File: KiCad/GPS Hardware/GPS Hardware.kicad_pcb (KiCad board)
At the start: 4 copper layers, 50 x 50 mm, 74 parts, among them J1 USB_C_Receptacle_USB2.0, J2 Conn_01x06_Male, J3 Conn_Coaxial, J4 SIM8051-6-0-14-01-X-REVD, J5 B2B-XH-A(LF)(SN), Q1 BC847, Q2 BC847, Q3 BSS84, U1 ESD122DMX, U10 ublox_SAM-M8Q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

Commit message: Update to PC
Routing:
- net VCC_GPS: track 29.3 -> 33.1 mm

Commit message: Update to laptop
You need to finish gnd via placement
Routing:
- net Net-(J1-PadB5): track 0.00 -> 2.69 mm
- net GND: vias 22 -> 23
- net D-: vias 0 -> 1

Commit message: Update to PC Remember to double-check pads
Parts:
- moved C31 0.76 mm to (118.7, 64.3)
- moved D6 0.55 mm to (119.9, 64.2)
- moved C30 0.52 mm to (120.8, 64.2)
- moved TH1 0.32 mm to (103.5, 71.9)
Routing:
- net GND: track 13.0 -> 21.9 mm, vias 23 -> 111
- net D+: track 4.98 -> 10.2 mm
- net D-: track 5.93 -> 8.94 mm, vias 1 -> 2
- net Net-(C10-Pad1): track 0.00 -> 2.09 mm
- net VSIM: track 26.9 -> 25.3 mm
- net SCL_Power: track 84.0 -> 85.1 mm
- net SDA_Power: track 81.5 -> 82.5 mm
- net INT_Power: track 62.3 -> 63.1 mm
- net +3V3: vias 8 -> 10

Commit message: Update from laptop
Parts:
- moved C28 0.51 mm to (134.6, 62.9)
- moved D4 0.51 mm to (135.6, 62.9)
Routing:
- net +3V3: track 10.3 -> 13.8 mm, vias 10 -> 14
- net VCC_GPS: track 33.1 -> 36.4 mm
- net GND: track 21.9 -> 23.9 mm, vias 111 -> 114

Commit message: Update from university
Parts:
- moved TH1 0.22 mm to (103.3, 71.9)
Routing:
- net Net-(J3-Pad1): track 0.00 -> 3.82 mm
- net GND: track 23.9 -> 22.6 mm, vias 114 -> 177
- net CLK: track 41.6 -> 40.5 mm
- net RESET_Cellular: vias 2 -> 3

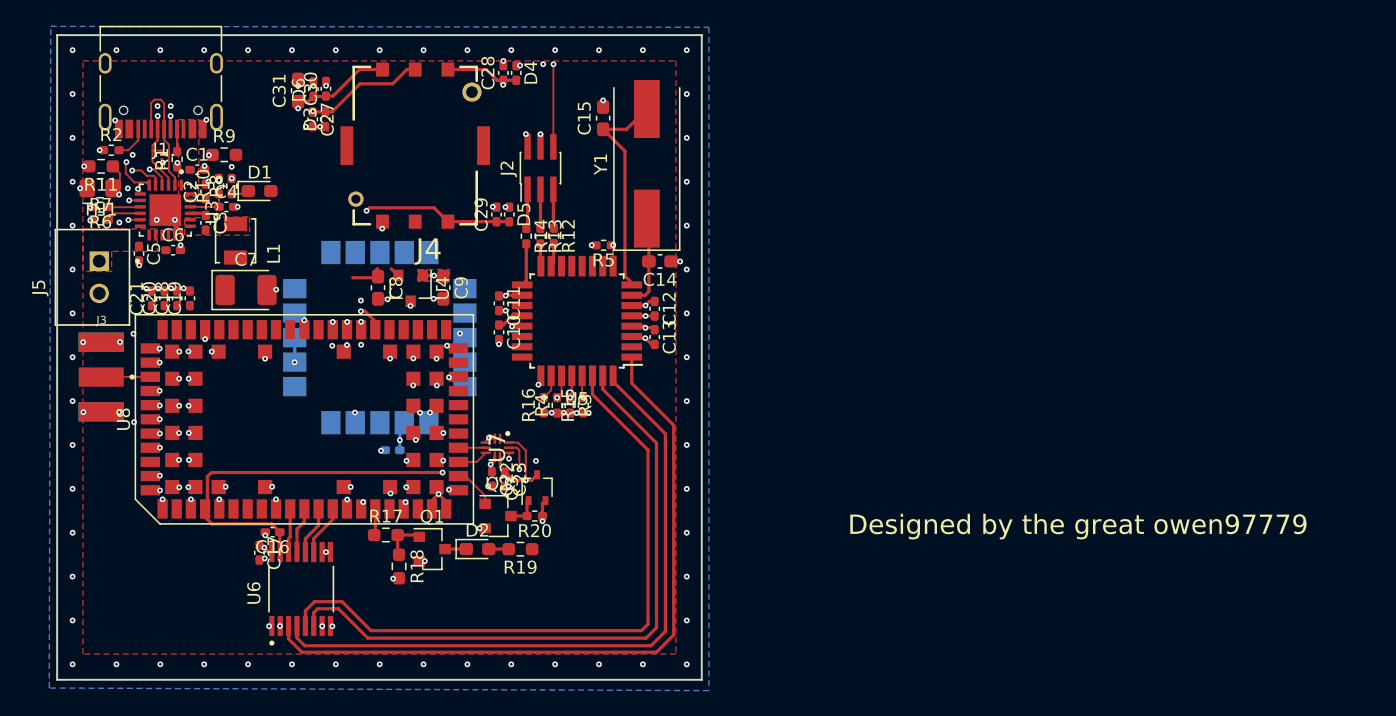
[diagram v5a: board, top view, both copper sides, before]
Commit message: Updated silkscreen
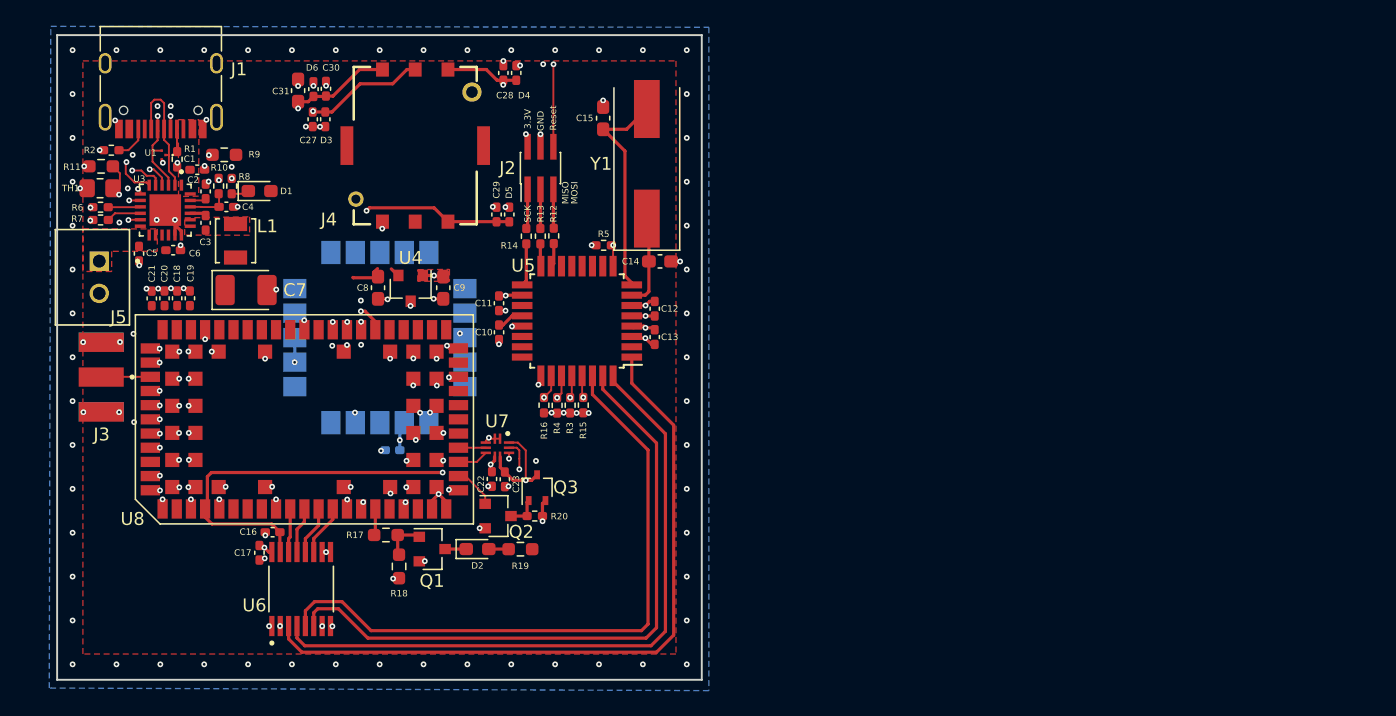
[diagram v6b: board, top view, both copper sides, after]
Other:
- board text added: "3.3V"
- board text added: "Designed by Owen97779 and Alexyodude"
- board text added: "GND"
- board text added: "MISO"
- board text added: "MOSI"
- board text added: "Reset"
- board text added: "SCK"
- board text added: "v1.0"
- board text removed: "Designed by the great owen97779"

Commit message: Finishing touches
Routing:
- net GND: track 22.6 -> 21.8 mm, vias 177 -> 186
- net EXTINT: track 17.6 -> 18.3 mm
- net RESET_Cellular: vias 3 -> 2
- net +3V3: vias 14 -> 15

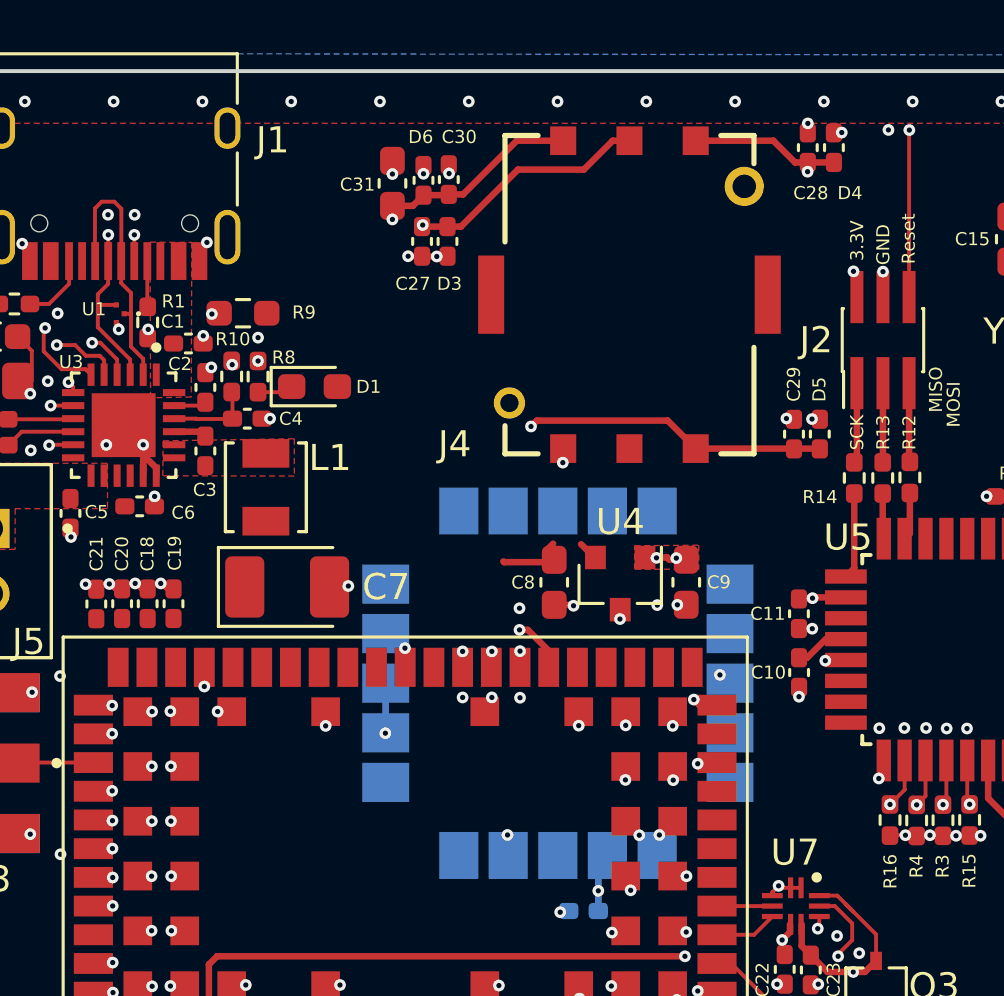
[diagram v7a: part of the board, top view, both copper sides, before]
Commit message: Changed via placement and all that jazz
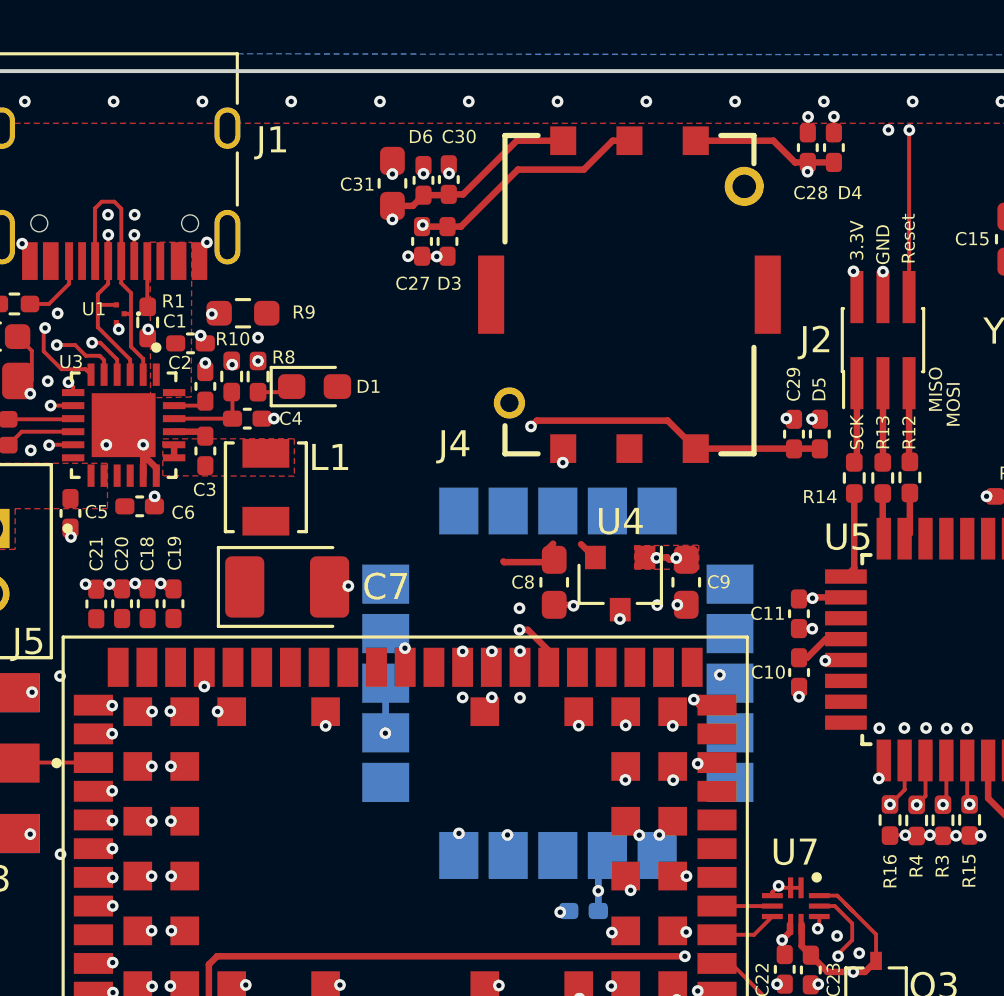
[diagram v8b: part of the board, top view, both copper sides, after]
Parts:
- moved C1 0.08 mm to (111.0, 70.4)
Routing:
- net GND: track 21.8 -> 23.5 mm, vias 186 -> 187
- net Net-(C3-Pad2): track 0.00 -> 0.50 mm
